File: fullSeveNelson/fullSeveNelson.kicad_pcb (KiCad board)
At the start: 2 copper layers, 285 x 94.6 mm, 139 parts, among them J1 USB_C_Receptacle_USB2.0, U1 STM32F072CBT6, U2 PRTR5V0U2X, U3 XC6206PxxxMR-Regulator_Linear

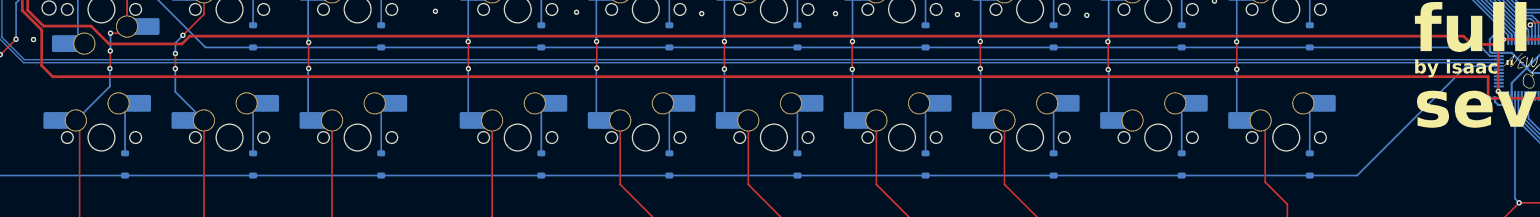
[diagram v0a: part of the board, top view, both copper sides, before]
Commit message: updated fills
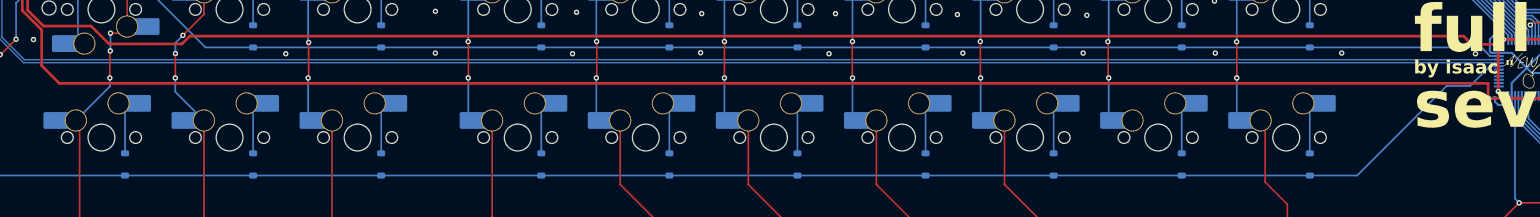
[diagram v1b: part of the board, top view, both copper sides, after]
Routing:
- net GND: track 386.2 -> 385.6 mm, vias 18 -> 28

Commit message: fixed spacing and mounting holes
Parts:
- removed ?: , 
- added REF**: MountingHole_2.1mm, MountingHole:MountingHole_2.1mm, F.Cu at (227.7, 172.6)
- moved D13 4.76 mm to (462.8, 157.7)
- moved D47 4.76 mm to (462.8, 214.9)
- moved D57 4.76 mm to (462.8, 233.9)
- moved MX13 4.76 mm to (459.3, 153.7)
- moved MX47 4.76 mm to (459.3, 210.9)
- moved MX57 4.76 mm to (459.3, 229.9)
- moved BOOT1 4.76 mm to (469.2, 178.5)
- moved C1 4.76 mm to (460.0, 183.0)
- moved C3 4.76 mm to (447.7, 177.2)
- moved C4 4.76 mm to (448.0, 186.0)
- moved C5 4.76 mm to (456.5, 177.0)
- moved C6 4.76 mm to (458.0, 177.5)
- moved C7 4.76 mm to (458.7, 183.0)
- moved D12 4.76 mm to (443.8, 157.7)
- moved D14 4.76 mm to (481.9, 157.7)
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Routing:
- net GND: track 385.6 -> 390.8 mm
- net +3V3: track 293.0 -> 297.7 mm
- net D-: track 252.9 -> 257.7 mm
- net D+: track 253.8 -> 258.6 mm
- net ROW2: track 234.9 -> 239.6 mm
- net ROW3: track 305.4 -> 310.1 mm
- net ROW1: track 242.1 -> 246.8 mm
- net COL0: track 337.6 -> 342.3 mm
- net ROW4: track 335.9 -> 339.2 mm
- net COL3: track 270.1 -> 273.3 mm
- net COL2: track 304.8 -> 307.9 mm
- net COL1: track 305.4 -> 308.5 mm
- net ROW0: track 287.7 -> 290.9 mm
- net COL8: track 170.2 -> 171.8 mm
- net COL6: track 189.2 -> 190.8 mm
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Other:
- outline, holes or cut-outs redrawn
